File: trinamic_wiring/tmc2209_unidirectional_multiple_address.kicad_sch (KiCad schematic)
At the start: 6 parts

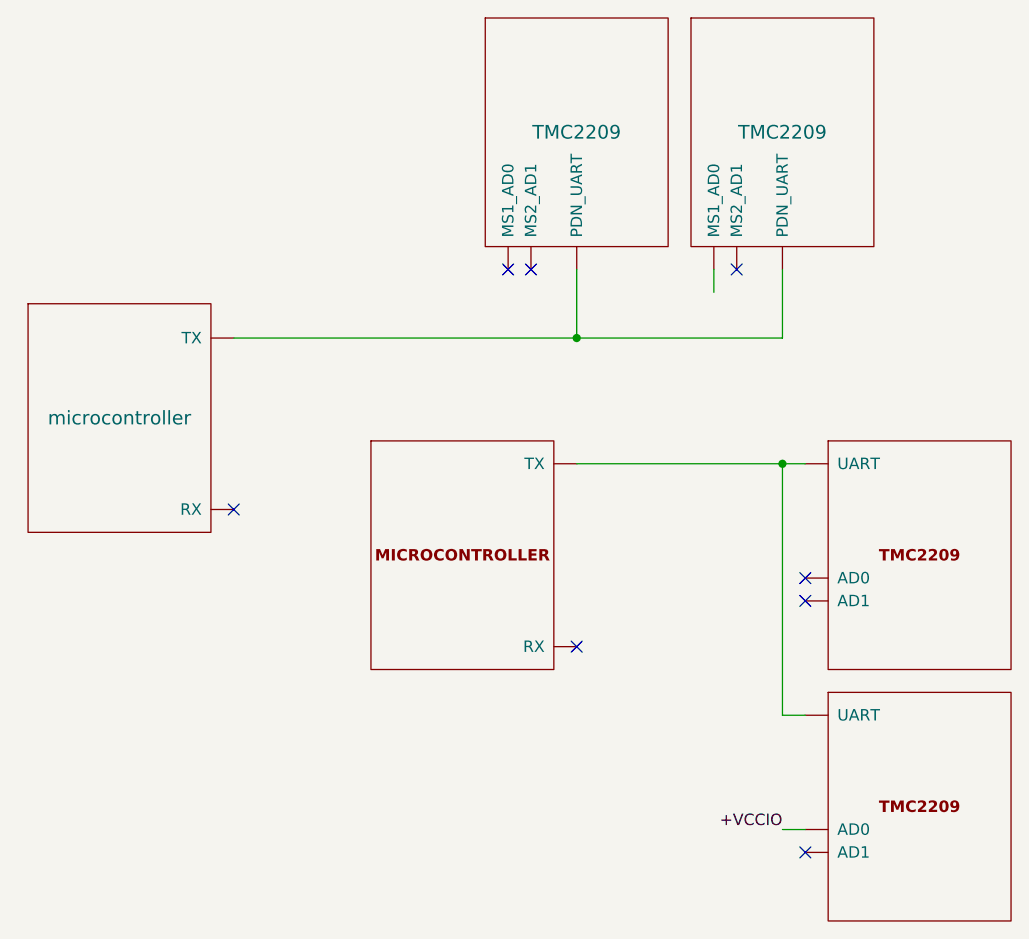
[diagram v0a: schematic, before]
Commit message: Add more schematics
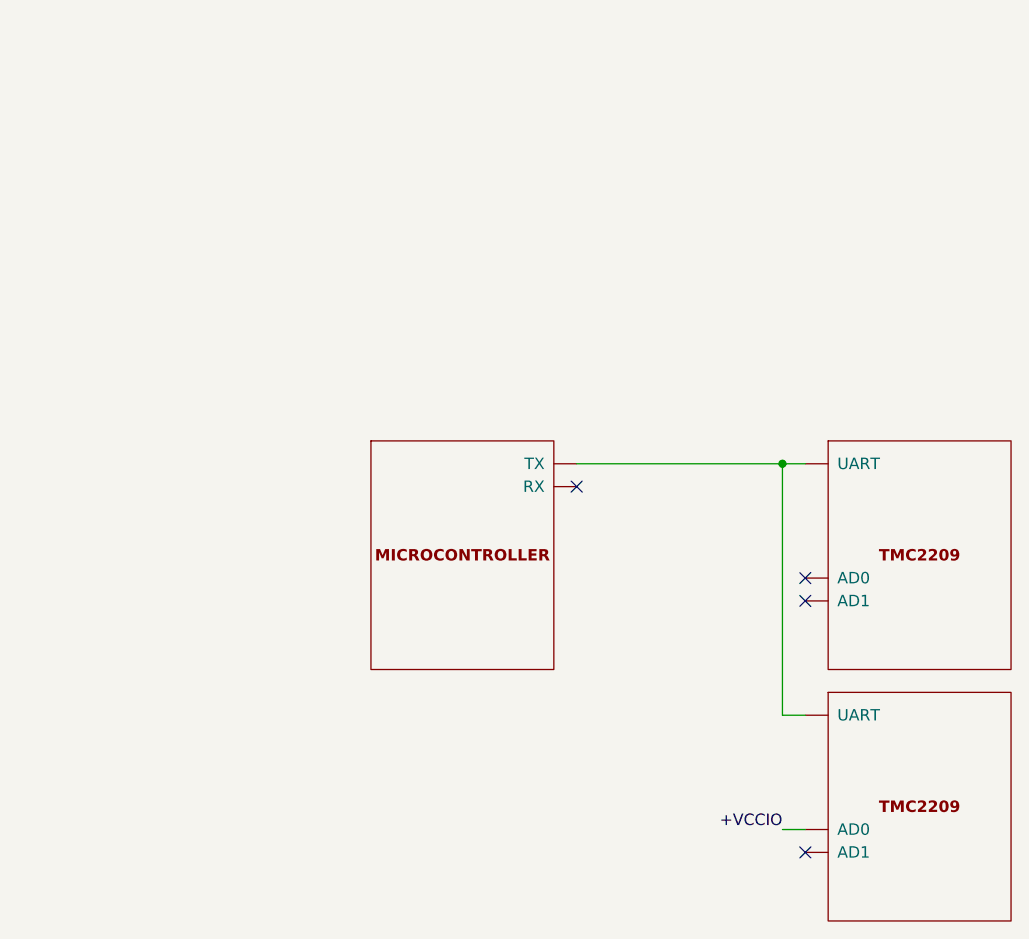
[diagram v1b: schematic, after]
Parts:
- removed MICROCONTROLLER4: DOC_MCU_UART, symbol Janelia:DOC_MCU_UART
- removed TMC2, TMC3: TMC2209, symbol Janelia:SIMPLIFIED_TMC2209_ADDRESSES
- removed microcontroller?: microcontroller, symbol Janelia:SIMPLIFIED_MCU_UART
- added MICROCONTROLLER4: DOC_MCU, symbol Janelia:DOC_MCU
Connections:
- net at TMC6.0 (UART), TMC6.0 (UART): now also MICROCONTROLLER4.1 (TX)
- no-connect marks 8 -> 4
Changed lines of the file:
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@@
   (title_block
     (title "Trinamic Wiring")
-    (date "2023-08-01")
+    (date "2023-08-02")
     (rev "0.4")
     (company "Janelia Research Campus")
   )
-  (junction (at 138.43 87.63) (diameter 0) (color 0 0 0 0)
-  )
   (junction (at 161.29 101.6) (diameter 0) (color 0 0 0 0)
   )
-  (no_connect (at 133.35 80.01))
-  (no_connect (at 130.81 80.01))
   (no_connect (at 163.83 116.84))
   (no_connect (at 163.83 114.3))
-  (no_connect (at 138.43 121.92))
+  (no_connect (at 138.43 104.14))
   (no_connect (at 163.83 144.78))
-  (no_connect (at 156.21 80.01))
-  (no_connect (at 100.33 106.68))
   (wire (pts (xy 161.29 101.6) (xy 161.29 129.54))
     (stroke (width 0) (type default))
   )
-  (wire (pts (xy 138.43 87.63) (xy 161.29 87.63))
-    (stroke (width 0) (type default))
-  )
-  (wire (pts (xy 100.33 87.63) (xy 138.43 87.63))
-    (stroke (width 0) (type default))
-  )
   (wire (pts (xy 138.43 101.6) (xy 161.29 101.6))
-    (stroke (width 0) (type default))
-  )
-  (wire (pts (xy 153.67 80.01) (xy 153.67 82.55))
     (stroke (width 0) (type default))
   )
@@
     (stroke (width 0) (type default))
   )
-  (wire (pts (xy 138.43 80.01) (xy 138.43 87.63))
-    (stroke (width 0) (type default))
-  )
-  (wire (pts (xy 161.29 80.01) (xy 161.29 87.63))
-    (stroke (width 0) (type default))
-  )
   (label "+VCCIO" (at 161.29 142.24 180) (fields_autoplaced)
-    (effects (font (size 1.27 1.27) (color 255 0 255 1)) (justify right bottom))
-  )
-  (symbol (lib_id "Janelia:DOC_MCU_UART") (at 125.73 111.76 0) (unit 1)
-    (in_bom yes) (on_board yes) (dnp no) (fields_autoplaced)
-    (property "Reference" "MICROCONTROLLER4" (at 125.73 92.71 0) (do_not_autoplace)
-      (effects (font (size 1.27 1.27)) hide)
-    )
-    (property "Value" "DOC_MCU_UART" (at 125.73 97.79 0)
-      (effects (font (size 1.524 1.524)) hide)
-    )
-    (property "Footprint" "" (at 123.19 138.43 0)
-      (effects (font (size 1.524 1.524)) hide)
-    )
-    (property "Datasheet" "" (at 125.73 111.76 0)
-      (effects (font (size 1.524 1.524)) hide)
-    )
-    (property "Sim.Enable" "0" (at 125.73 95.25 0)
-      (effects (font (size 1.27 1.27)) hide)
-    )
-    (pin "0")
-    (pin "1")
-    (instances
-      (project "trinamic_wiring"
-        (path "/e4144788-6304-493f-818e-5d881d3b7418/c8eda2b5-ab13-4033-82d9-875c9fcaf884/13e2a7b5-46df-44bb-8dde-5d79d190b8bf"
-          (reference "MICROCONTROLLER4") (unit 1)
-        )
-        (path "/e4144788-6304-493f-818e-5d881d3b7418/c8eda2b5-ab13-4033-82d9-875c9fcaf884/5b0a2695-6b0b-4c82-b9d6-7e19fee75501"
-          (reference "MICROCONTROLLER1") (unit 1)
-        )
-        (path "/e4144788-6304-493f-818e-5d881d3b7418/c8eda2b5-ab13-4033-82d9-875c9fcaf884/a2ce530e-f5b5-4e3e-9188-e4bc8f84c739"
-          (reference "MICROCONTROLLER3") (unit 1)
-        )
-      )
-    )
-  )
-  (symbol (lib_id "Janelia:SIMPLIFIED_MCU_UART") (at 87.63 96.52 0) (unit 1)
-    (in_bom yes) (on_board yes) (dnp no)
-    (property "Reference" "microcontroller?" (at 87.63 96.52 0) (do_not_autoplace)
-      (effects (font (size 1.524 1.524)) hide)
-    )
-    (property "Value" "microcontroller" (at 87.63 96.52 0)
-      (effects (font (size 1.524 1.524)))
-    )
-    (property "Footprint" "" (at 85.09 123.19 0)
-      (effects (font (size 1.524 1.524)) hide)
-    )
-    (property "Datasheet" "" (at 87.63 96.52 0)
-      (effects (font (size 1.524 1.524)) hide)
-    )
-    (pin "0")
-    (pin "1")
-    (instances
-      (project "trinamic_wiring"
-        (path "/e4144788-6304-493f-818e-5d881d3b7418/c8eda2b5-ab13-4033-82d9-875c9fcaf884/13e2a7b5-46df-44bb-8dde-5d79d190b8bf"
-          (reference "microcontroller?") (unit 1)
-        )
-        (path "/e4144788-6304-493f-818e-5d881d3b7418/c8eda2b5-ab13-4033-82d9-875c9fcaf884/e3613d8e-f506-47d6-ad2d-b0f5798d9847"
-          (reference "microcontroller1") (unit 1)
-        )
-        (path "/e4144788-6304-493f-818e-5d881d3b7418/c8eda2b5-ab13-4033-82d9-875c9fcaf884/5f6f310d-167d-42a3-8815-1b623fe73dc8"
-          (reference "microcontroller2") (unit 1)
-        )
-        (path "/e4144788-6304-493f-818e-5d881d3b7418/c8eda2b5-ab13-4033-82d9-875c9fcaf884/a2ce530e-f5b5-4e3e-9188-e4bc8f84c739"
-          (reference "microcontroller?") (unit 1)
-        )
-      )
-    )
+    (effects (font (size 1.27 1.27)) (justify right bottom))
   )
   (symbol (lib_id "Janelia:DOC_TMC2209") (at 176.53 139.7 0) (unit 1)
@@
         (path "/e4144788-6304-493f-818e-5d881d3b7418/c8eda2b5-ab13-4033-82d9-875c9fcaf884/a2ce530e-f5b5-4e3e-9188-e4bc8f84c739"
           (reference "TMC5") (unit 1)
-        )
-      )
-    )
-  )
-  (symbol (lib_id "Janelia:SIMPLIFIED_TMC2209_ADDRESSES") (at 138.43 64.77 0) (unit 1)
-    (in_bom yes) (on_board yes) (dnp no)
-    (property "Reference" "TMC2" (at 138.43 64.77 0) (do_not_autoplace)
-      (effects (font (size 1.524 1.524)) hide)
-    )
-    (property "Value" "TMC2209" (at 138.43 64.77 0) (do_not_autoplace)
-      (effects (font (size 1.524 1.524)))
-    )
-    (property "Footprint" "" (at 135.89 91.44 0)
-      (effects (font (size 1.524 1.524)) hide)
-    )
-    (property "Datasheet" "" (at 138.43 64.77 0)
-      (effects (font (size 1.524 1.524)) hide)
-    )
-    (pin "0")
-    (pin "1")
-    (pin "2")
-    (instances
-      (project "trinamic_wiring"
-        (path "/e4144788-6304-493f-818e-5d881d3b7418/c8eda2b5-ab13-4033-82d9-875c9fcaf884/5f6f310d-167d-42a3-8815-1b623fe73dc8"
-          (reference "TMC2") (unit 1)
-        )
-        (path "/e4144788-6304-493f-818e-5d881d3b7418/c8eda2b5-ab13-4033-82d9-875c9fcaf884/a2ce530e-f5b5-4e3e-9188-e4bc8f84c739"
-          (reference "TMC2") (unit 1)
-        )
-      )
-    )
-  )
-  (symbol (lib_id "Janelia:SIMPLIFIED_TMC2209_ADDRESSES") (at 161.29 64.77 0) (unit 1)
-    (in_bom yes) (on_board yes) (dnp no)
-    (property "Reference" "TMC3" (at 161.29 64.77 0) (do_not_autoplace)
-      (effects (font (size 1.524 1.524)) hide)
-    )
-    (property "Value" "TMC2209" (at 161.29 64.77 0) (do_not_autoplace)
-      (effects (font (size 1.524 1.524)))
-    )
-    (property "Footprint" "" (at 158.75 91.44 0)
-      (effects (font (size 1.524 1.524)) hide)
-    )
-    (property "Datasheet" "" (at 161.29 64.77 0)
-      (effects (font (size 1.524 1.524)) hide)
-    )
-    (pin "0")
-    (pin "1")
-    (pin "2")
-    (instances
-      (project "trinamic_wiring"
-        (path "/e4144788-6304-493f-818e-5d881d3b7418/c8eda2b5-ab13-4033-82d9-875c9fcaf884/5f6f310d-167d-42a3-8815-1b623fe73dc8"
-          (reference "TMC3") (unit 1)
-        )
-        (path "/e4144788-6304-493f-818e-5d881d3b7418/c8eda2b5-ab13-4033-82d9-875c9fcaf884/a2ce530e-f5b5-4e3e-9188-e4bc8f84c739"
-          (reference "TMC3") (unit 1)
         )
       )
@@
         )
       )
+    )
+  )
+  (symbol (lib_id "Janelia:DOC_MCU") (at 125.73 111.76 0) (unit 1)
+    (in_bom yes) (on_board yes) (dnp no) (fields_autoplaced)
+    (property "Reference" "MICROCONTROLLER4" (at 125.73 92.71 0)
+      (effects (font (size 1.27 1.27)) hide)
+    )
+    (property "Value" "DOC_MCU" (at 125.73 97.79 0)
+      (effects (font (size 1.524 1.524)) hide)
+    )
+    (property "Footprint" "" (at 123.19 138.43 0)
+      (effects (font (size 1.524 1.524)) hide)
+    )
+    (property "Datasheet" "" (at 125.73 111.76 0)
+      (effects (font (size 1.524 1.524)) hide)
+    )
+    (property "Sim.Enable" "0" (at 125.73 95.25 0)
+      (effects (font (size 1.27 1.27)) hide)
+    )
+    (pin "0")
+    (pin "1")
+    (pin "2")
+    (pin "3")
+    (pin "4")
+    (pin "5")
+    (pin "6")
+    (pin "7")
+    (pin "8")
+    (instances
+      (project "trinamic_wiring"
+        (path "/e4144788-6304-493f-818e-5d881d3b7418/c8eda2b5-ab13-4033-82d9-875c9fcaf884/13e2a7b5-46df-44bb-8dde-5d79d190b8bf"
+          (reference "MICROCONTROLLER4") (unit 1)
+        )
+        (path "/e4144788-6304-493f-818e-5d881d3b7418/c8eda2b5-ab13-4033-82d9-875c9fcaf884/5b0a2695-6b0b-4c82-b9d6-7e19fee75501"
+          (reference "MICROCONTROLLER1") (unit 1)
+        )
+        (path "/e4144788-6304-493f-818e-5d881d3b7418/c8eda2b5-ab13-4033-82d9-875c9fcaf884/a2ce530e-f5b5-4e3e-9188-e4bc8f84c739"
+          (reference "MICROCONTROLLER3") (unit 1)
+        )
+      )
